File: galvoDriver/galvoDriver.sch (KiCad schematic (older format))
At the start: 26 parts, among them U1 LM358, U2 LM358, U3 LM358

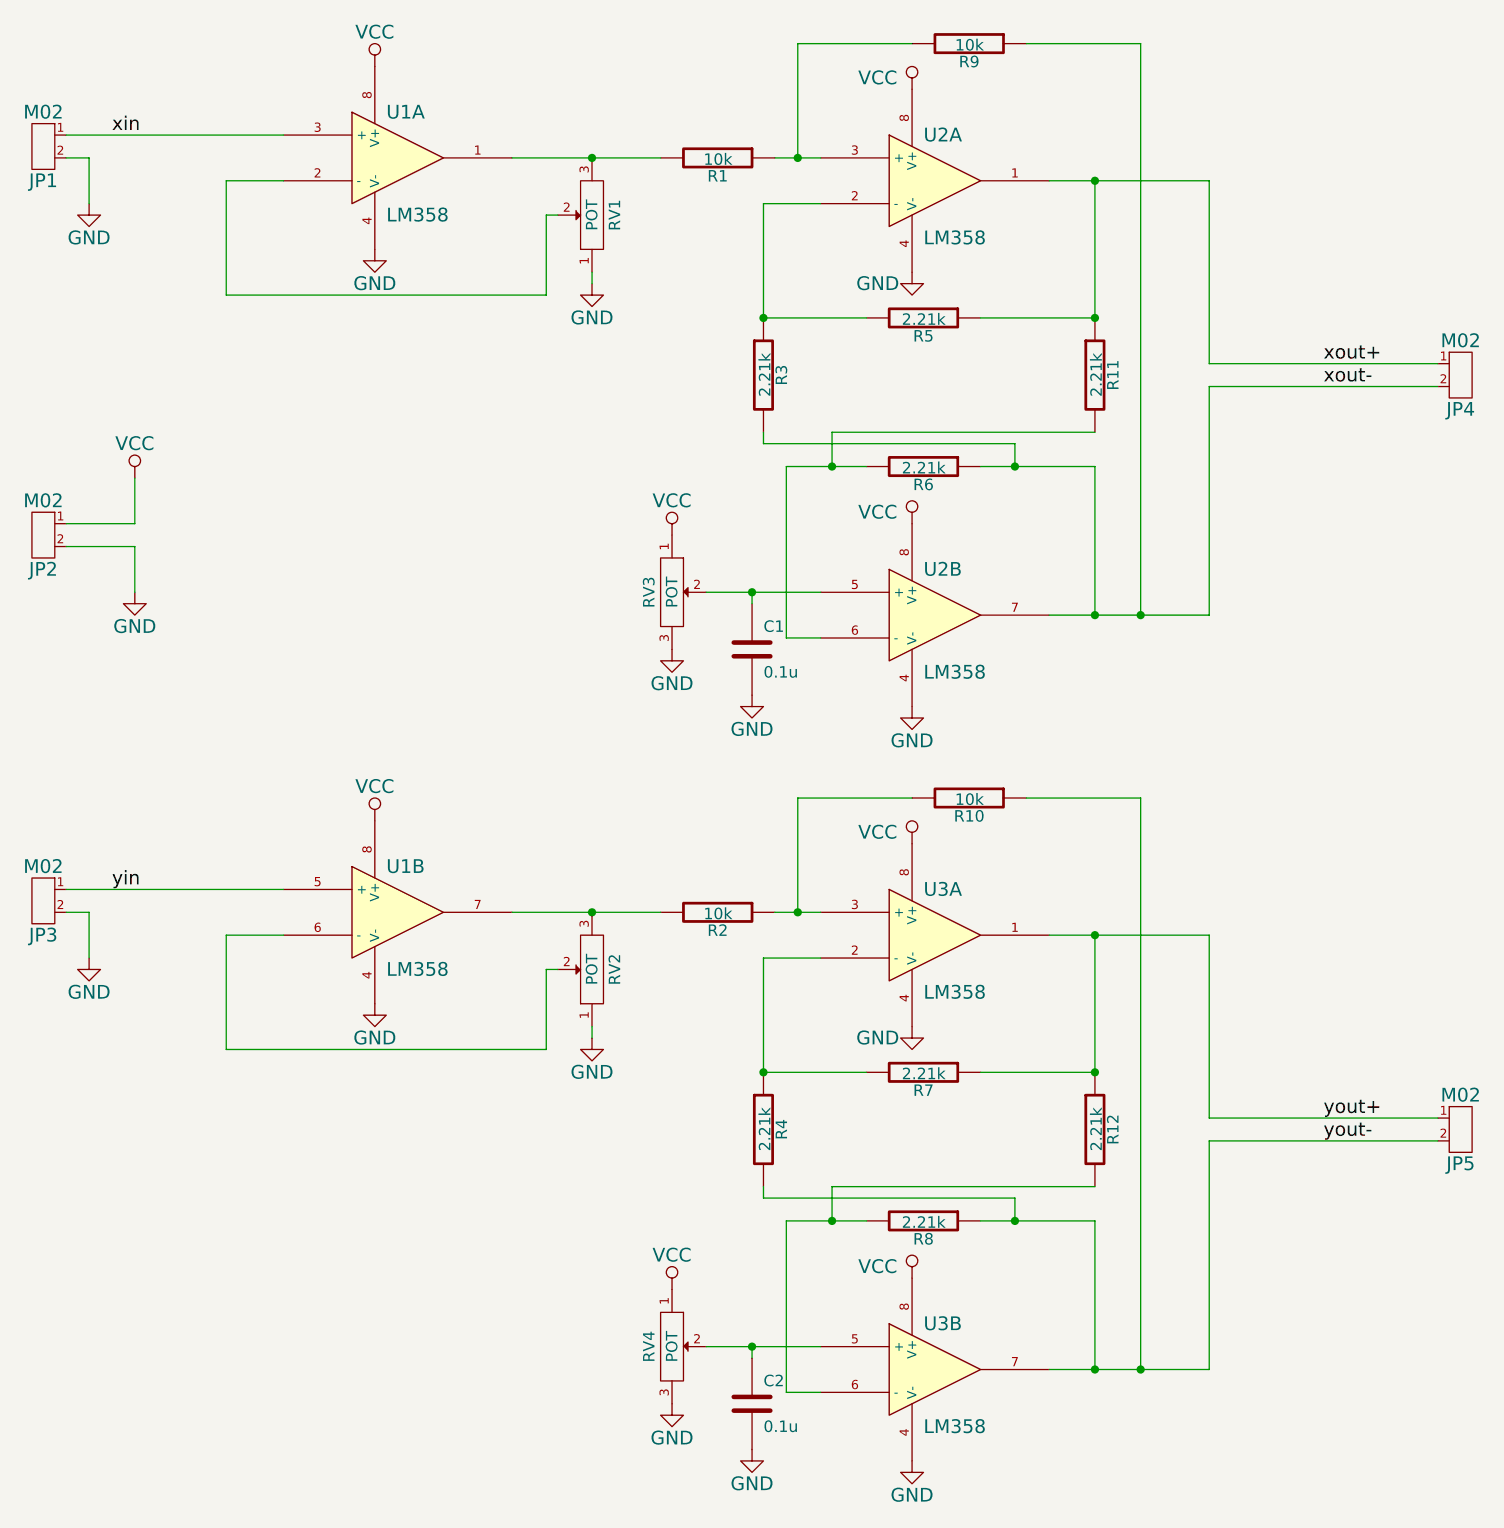
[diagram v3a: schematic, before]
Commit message: Added footprints
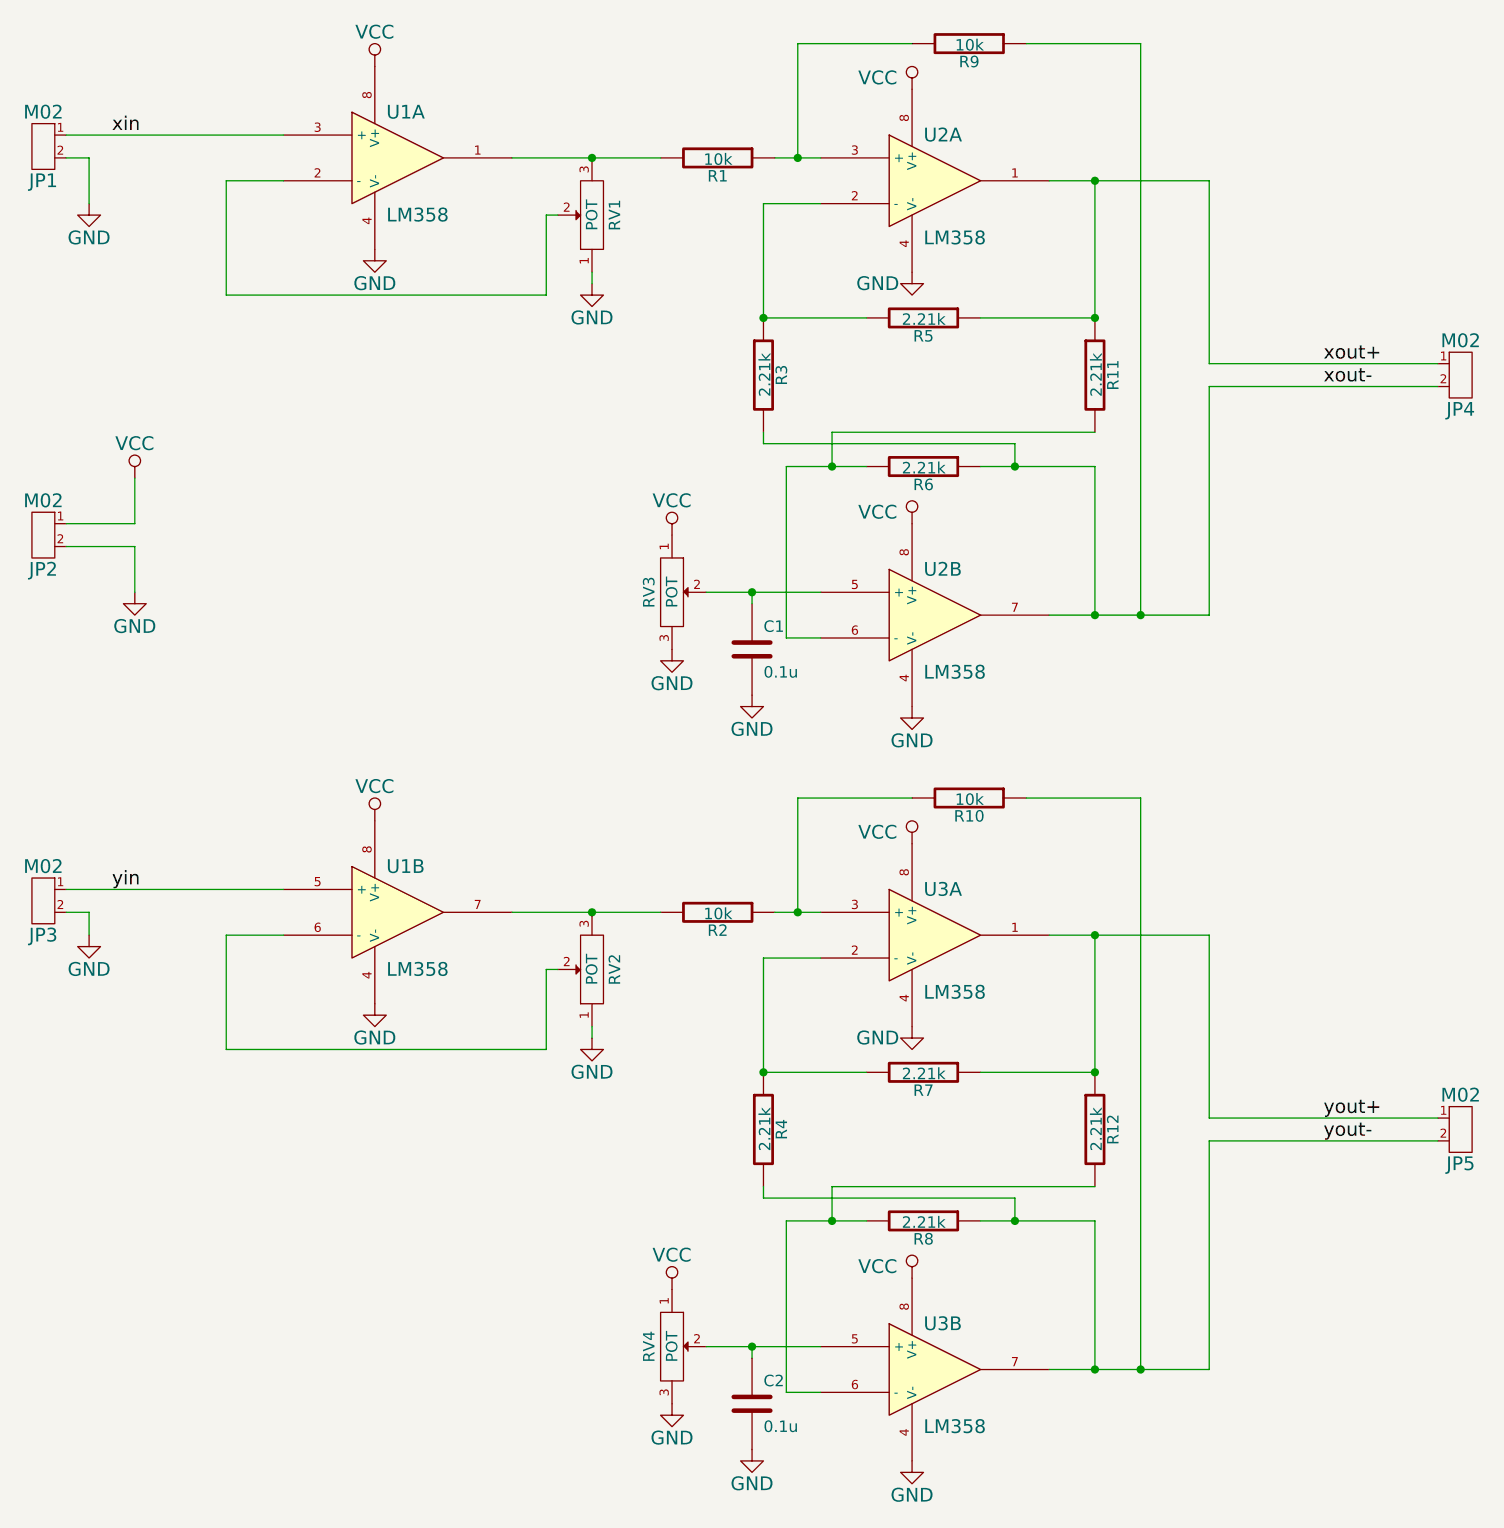
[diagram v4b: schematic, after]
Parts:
- C1, C2: footprint (none) -> Capacitors_SMD:C_0805
- JP1, JP2, JP3, JP4, JP5: footprint (none) -> Pin_Headers:Pin_Header_Straight_1x02
- R1, R10, R11, R12, R2, R3, R4, R5, R6, R7, R8, R9: footprint (none) -> Resistors_SMD:R_0805
- RV1, RV2, RV3, RV4: footprint (none) -> alvarop:POT-4mm
- U1, U2, U3: footprint (none) -> Housings_SOIC:SOIC-8_3.9x4.9mm_Pitch1.27mm

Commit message: Flipped amplifiers
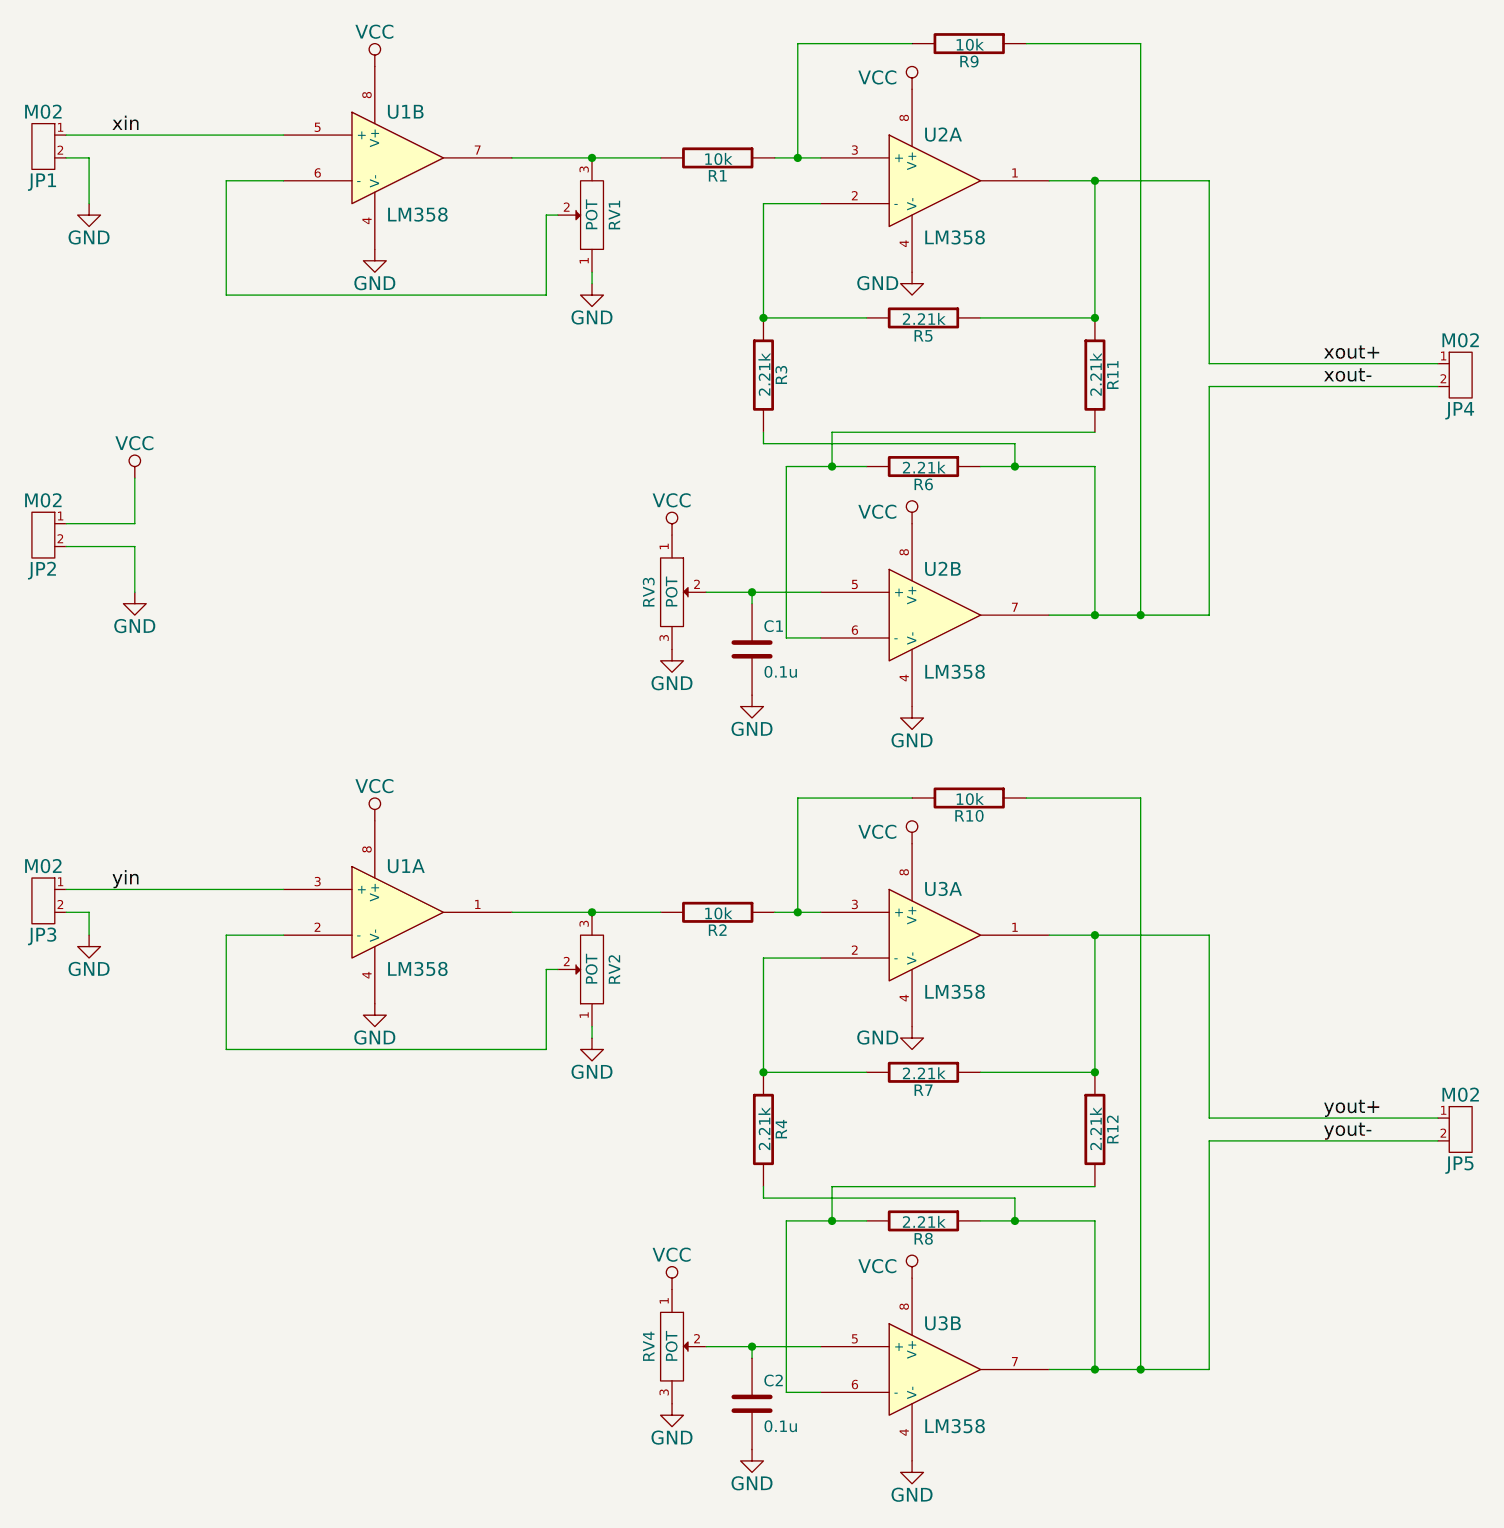
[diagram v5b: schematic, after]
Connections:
- net xin: now also U1.5 (+); no longer U1.3 (+)
- net yin: now also U1.3 (+); no longer U1.5 (+)
- net at R1.2, RV1.3: now also U1.7; no longer U1.1
- net at U1.2 (-): now also RV2.2; no longer RV1.2
- net at U1.6 (-): now also RV1.2; no longer RV2.2
- net at R2.2, RV2.3: now also U1.1; no longer U1.7
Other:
- moved on the sheet: U1A, U1B
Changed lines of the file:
@@
 L LM358 U1
 U 1 1 55A29DAF
+P 4250 4500
+F 0 "U1" H 4200 4700 60  0000 L CNN
+F 1 "LM358" H 4200 4250 60  0000 L CNN
+F 2 "Housings_SOIC:SOIC-8_3.9x4.9mm_Pitch1.27mm" H 4250 4500 60  0001 C CNN
+F 3 "" H 4250 4500 60  0000 C CNN
+	1    4250 4500
+	1    0    0    -1
+$EndComp
+$Comp
+L LM358 U1
+U 2 1 55A29DC6
 P 4250 1200
 F 0 "U1" H 4200 1400 60  0000 L CNN
@@
 F 2 "Housings_SOIC:SOIC-8_3.9x4.9mm_Pitch1.27mm" H 4250 1200 60  0001 C CNN
 F 3 "" H 4250 1200 60  0000 C CNN
-	1    4250 1200
-	1    0    0    -1
-$EndComp
-$Comp
-L LM358 U1
-U 2 1 55A29DC6
-P 4250 4500
-F 0 "U1" H 4200 4700 60  0000 L CNN
-F 1 "LM358" H 4200 4250 60  0000 L CNN
-F 2 "Housings_SOIC:SOIC-8_3.9x4.9mm_Pitch1.27mm" H 4250 4500 60  0001 C CNN
-F 3 "" H 4250 4500 60  0000 C CNN
-	2    4250 4500
+	2    4250 1200
 	1    0    0    -1
 $EndComp
@@
 Connection ~ 5100 1200
 Wire Wire Line
-	4750 1200 5400 1200
+	4750 1200 5100 1200
+Wire Wire Line
+	5100 1200 5400 1200
 Connection ~ 5800 3100
 Wire Wire Line
 	5800 3150 5800 3100
 Wire Wire Line
-	5600 3100 6100 3100
+	5600 3100 5800 3100
+Wire Wire Line
+	5800 3100 6100 3100
 Wire Wire Line
 	7500 3200 7500 700
@@
 	6150 2550 6150 2400
 Wire Wire Line
-	5950 2550 6300 2550
+	5950 2550 6150 2550
+Wire Wire Line
+	6150 2550 6300 2550
 Connection ~ 6950 2550
 Wire Wire Line
@@
 	5850 2400 5850 2450
 Wire Wire Line
-	7100 3200 7800 3200
+	7100 3200 7300 3200
+Wire Wire Line
+	7300 3200 7500 3200
+Wire Wire Line
+	7500 3200 7800 3200
 Wire Wire Line
 	7300 2550 7300 3200
 Wire Wire Line
-	6800 2550 7300 2550
+	6800 2550 6950 2550
+Wire Wire Line
+	6950 2550 7300 2550
 Connection ~ 7300 1300
 Connection ~ 7300 1900
 Wire Wire Line
-	7100 1300 7800 1300
+	7100 1300 7300 1300
+Wire Wire Line
+	7300 1300 7800 1300
 Wire Wire Line
 	7300 1300 7300 1900
@@
 Connection ~ 6000 1200
 Wire Wire Line
-	5900 1200 6100 1200
+	5900 1200 6000 1200
+Wire Wire Line
+	6000 1200 6100 1200
 Wire Wire Line
 	4950 1450 4900 1450
@@
 Connection ~ 5100 4500
 Wire Wire Line
-	4750 4500 5400 4500
+	4750 4500 5100 4500
+Wire Wire Line
+	5100 4500 5400 4500
 Connection ~ 5800 6400
 Wire Wire Line
 	5800 6450 5800 6400
 Wire Wire Line
-	5600 6400 6100 6400
+	5600 6400 5800 6400
+Wire Wire Line
+	5800 6400 6100 6400
 Wire Wire Line
 	7500 6500 7500 4000
@@
 	6150 5850 6150 5700
 Wire Wire Line
-	5950 5850 6300 5850
+	5950 5850 6150 5850
+Wire Wire Line
+	6150 5850 6300 5850
 Connection ~ 6950 5850
 Wire Wire Line
@@
 	5850 5700 5850 5750
 Wire Wire Line
-	7100 6500 7800 6500
+	7100 6500 7300 6500
+Wire Wire Line
+	7300 6500 7500 6500
+Wire Wire Line
+	7500 6500 7800 6500
 Wire Wire Line
 	7300 5850 7300 6500
 Wire Wire Line
-	6800 5850 7300 5850
+	6800 5850 6950 5850
+Wire Wire Line
+	6950 5850 7300 5850
 Connection ~ 7300 4600
 Connection ~ 7300 5200
 Wire Wire Line
-	7100 4600 7800 4600
+	7100 4600 7300 4600
+Wire Wire Line
+	7300 4600 7800 4600
 Wire Wire Line
 	7300 4600 7300 5200
@@
 Connection ~ 6000 4500
 Wire Wire Line
-	5900 4500 6100 4500
+	5900 4500 6000 4500
+Wire Wire Line
+	6000 4500 6100 4500
 Wire Wire Line
 	4950 4750 4900 4750

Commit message: Updated version of kicad (replaced old symbols, I think)
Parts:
- C1, C2: symbol C -> C-RESCUE-galvoDriver
- R1, R10, R11, R12, R2, R3, R4, R5, R6, R7, R8, R9: symbol R -> R-RESCUE-galvoDriver
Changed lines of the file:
@@
 EESchema Schematic File Version 2
+LIBS:galvoDriver-rescue
 LIBS:alvarop
 LIBS:power
@@
 $EndComp
 $Comp
-L R R1
+L R-RESCUE-galvoDriver R1
 U 1 1 55A29F9F
 P 5650 1200
@@
 $EndComp
 $Comp
-L R R11
+L R-RESCUE-galvoDriver R11
 U 1 1 55A29FC6
 P 7300 2150
@@
 $EndComp
 $Comp
-L R R9
+L R-RESCUE-galvoDriver R9
 U 1 1 55A2A03F
 P 6750 700
@@
 $EndComp
 $Comp
-L R R6
+L R-RESCUE-galvoDriver R6
 U 1 1 55A2A099
 P 6550 2550
@@
 $EndComp
 $Comp
-L R R3
+L R-RESCUE-galvoDriver R3
 U 1 1 55A2A120
 P 5850 2150
@@
 $EndComp
 $Comp
-L R R5
+L R-RESCUE-galvoDriver R5
 U 1 1 55A2A15B
 P 6550 1900
@@
 $EndComp
 $Comp
-L C C1
+L C-RESCUE-galvoDriver C1
 U 1 1 55A2AE13
 P 5800 3350
@@
 $EndComp
 $Comp
-L R R2
+L R-RESCUE-galvoDriver R2
 U 1 1 55A2D700
 P 5650 4500
@@
 $EndComp
 $Comp
-L R R12
+L R-RESCUE-galvoDriver R12
 U 1 1 55A2D706
 P 7300 5450
@@
 $EndComp
 $Comp
-L R R10
+L R-RESCUE-galvoDriver R10
 U 1 1 55A2D70C
 P 6750 4000
@@
 $EndComp
 $Comp
-L R R8
+L R-RESCUE-galvoDriver R8
 U 1 1 55A2D712
 P 6550 5850
@@
 $EndComp
 $Comp
-L R R4
+L R-RESCUE-galvoDriver R4
 U 1 1 55A2D718
 P 5850 5450
@@
 $EndComp
 $Comp
-L R R7
+L R-RESCUE-galvoDriver R7
 U 1 1 55A2D71E
 P 6550 5200
@@
 $EndComp
 $Comp
-L C C2
+L C-RESCUE-galvoDriver C2
 U 1 1 55A2D724
 P 5800 6650
@@
 Connection ~ 5100 1200
 Wire Wire Line
-	4750 1200 5100 1200
-Wire Wire Line
-	5100 1200 5400 1200
+	4750 1200 5400 1200
 Connection ~ 5800 3100
 Wire Wire Line
 	5800 3150 5800 3100
 Wire Wire Line
-	5600 3100 5800 3100
-Wire Wire Line
-	5800 3100 6100 3100
+	5600 3100 6100 3100
 Wire Wire Line
 	7500 3200 7500 700
@@
 	6150 2550 6150 2400
 Wire Wire Line
-	5950 2550 6150 2550
-Wire Wire Line
-	6150 2550 6300 2550
+	5950 2550 6300 2550
 Connection ~ 6950 2550
 Wire Wire Line
@@
 	5850 2400 5850 2450
 Wire Wire Line
-	7100 3200 7300 3200
-Wire Wire Line
-	7300 3200 7500 3200
-Wire Wire Line
-	7500 3200 7800 3200
+	7100 3200 7800 3200
 Wire Wire Line
 	7300 2550 7300 3200
 Wire Wire Line
-	6800 2550 6950 2550
-Wire Wire Line
-	6950 2550 7300 2550
+	6800 2550 7300 2550
 Connection ~ 7300 1300
 Connection ~ 7300 1900
 Wire Wire Line
-	7100 1300 7300 1300
-Wire Wire Line
-	7300 1300 7800 1300
+	7100 1300 7800 1300
 Wire Wire Line
 	7300 1300 7300 1900
@@
 Connection ~ 6000 1200
 Wire Wire Line
-	5900 1200 6000 1200
-Wire Wire Line
-	6000 1200 6100 1200
+	5900 1200 6100 1200
 Wire Wire Line
 	4950 1450 4900 1450
@@
 Connection ~ 5100 4500
 Wire Wire Line
-	4750 4500 5100 4500
-Wire Wire Line
-	5100 4500 5400 4500
+	4750 4500 5400 4500
 Connection ~ 5800 6400
 Wire Wire Line
 	5800 6450 5800 6400
 Wire Wire Line
-	5600 6400 5800 6400
-Wire Wire Line
-	5800 6400 6100 6400
+	5600 6400 6100 6400
 Wire Wire Line
 	7500 6500 7500 4000
@@
 	6150 5850 6150 5700
 Wire Wire Line
-	5950 5850 6150 5850
-Wire Wire Line
-	6150 5850 6300 5850
+	5950 5850 6300 5850
 Connection ~ 6950 5850
 Wire Wire Line
@@
 	5850 5700 5850 5750
 Wire Wire Line
-	7100 6500 7300 6500
-Wire Wire Line
-	7300 6500 7500 6500
-Wire Wire Line
-	7500 6500 7800 6500
+	7100 6500 7800 6500
 Wire Wire Line
 	7300 5850 7300 6500
 Wire Wire Line
-	6800 5850 6950 5850
-Wire Wire Line
-	6950 5850 7300 5850
+	6800 5850 7300 5850
 Connection ~ 7300 4600
 Connection ~ 7300 5200
 Wire Wire Line
-	7100 4600 7300 4600
-Wire Wire Line
-	7300 4600 7800 4600
+	7100 4600 7800 4600
 Wire Wire Line
 	7300 4600 7300 5200
@@
 Connection ~ 6000 4500
 Wire Wire Line
-	5900 4500 6000 4500
-Wire Wire Line
-	6000 4500 6100 4500
+	5900 4500 6100 4500
 Wire Wire Line
 	4950 4750 4900 4750
